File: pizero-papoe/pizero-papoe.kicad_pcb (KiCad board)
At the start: 4 copper layers, 80 x 30 mm, 90 parts, among them IC1 RTL8153B-VB-CG, J1 PogoPin_01x01, J2 PogoPin_01x01, J3 PogoPin_01x01, J4 PogoPin_01x01, J5 PogoPin_01x01, J6 RJ45_LED_AK_Shielded, P1 USB_C_Plug_USB3.0_9P, Q2 DMMT3906_Dual_PNP, Q3 Q_PMOS_GSD, U1 93LC46B, U2 TPS63070RNMR, U3 MX25L3233FM1, U4 WE-TVS-82400102-dnp, Y1 25Mhz

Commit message: add JLC04162H-3313-stackup info
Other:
- board text added: "0"
- board text added: "0 mm"
- board text added: "0.01 mm"
- board text added: "0.0152 mm"
- board text added: "0.02"
- board text added: "0.035 mm"
- board text added: "0.0994 mm"
- board text added: "1"
- board text added: "1.265 mm"
- board text added: "3.3"
- board text added: "4.5"
- board text added: "B.Cu"
- board text added: "B.Mask"
- board text added: "B.Paste"
- board text added: "B.Silkscreen"
- board text added: "Bottom Silk Screen"
- board text added: "Bottom Solder Mask"
- board text added: "Bottom Solder Paste"
- board text added: "Color"
- board text added: "Dielectric 1"
- board text added: "Dielectric 2"
- board text added: "Dielectric 3"
- board text added: "Epsilon R"
- board text added: "F.Cu"
- board text added: "F.Mask"
- board text added: "F.Paste"
- board text added: "F.Silkscreen"
- board text added: "FR4"
- board text added: "In1.Cu"
- board text added: "In2.Cu"
- board text added: "Layer Name"
- board text added: "Loss Tangent"
- board text added: "Material"
- board text added: "Not specified"
- board text added: "Thickness (mm)"
- board text added: "Top Silk Screen"
- board text added: "Top Solder Mask"
- board text added: "Top Solder Paste"
- board text added: "Type"
- board text added: "copper"
- board text added: "core"
- board text added: "prepreg"

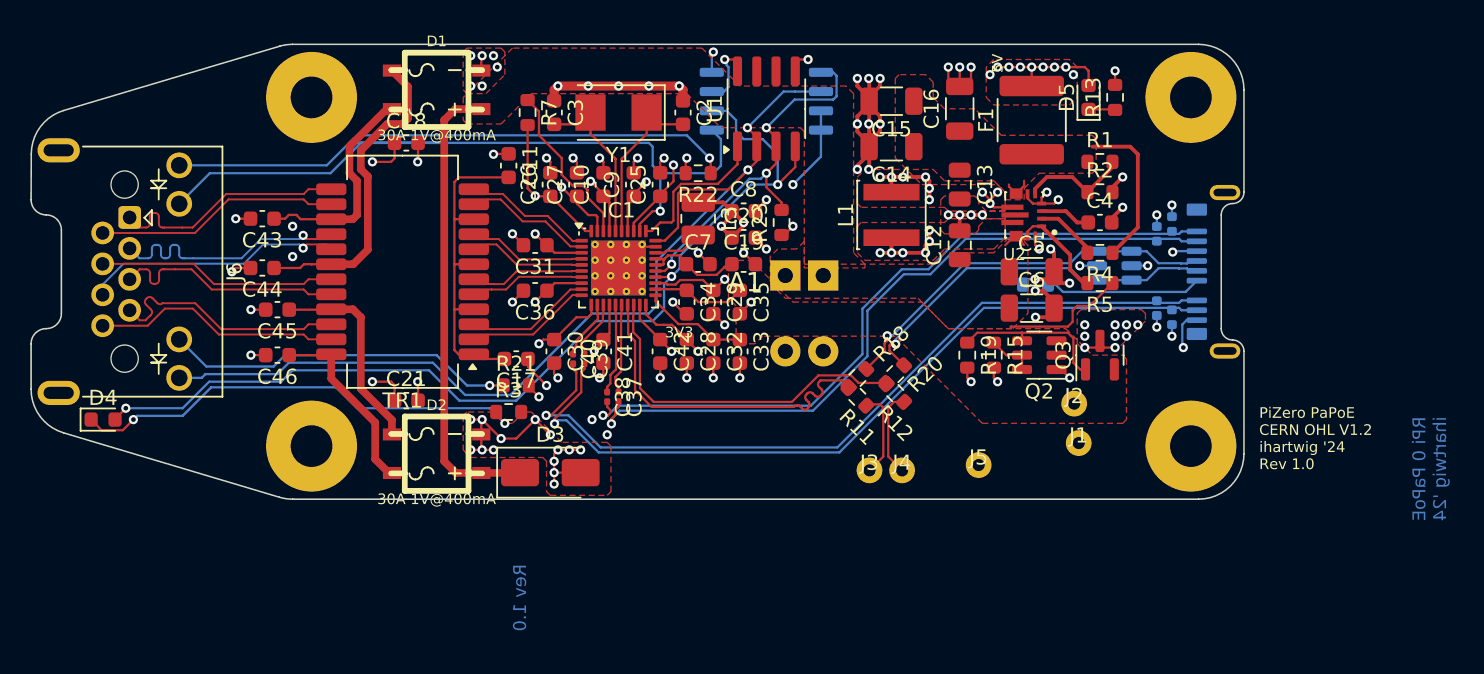
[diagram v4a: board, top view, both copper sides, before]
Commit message: pizero-papoe sch pcb fixes and cleanup
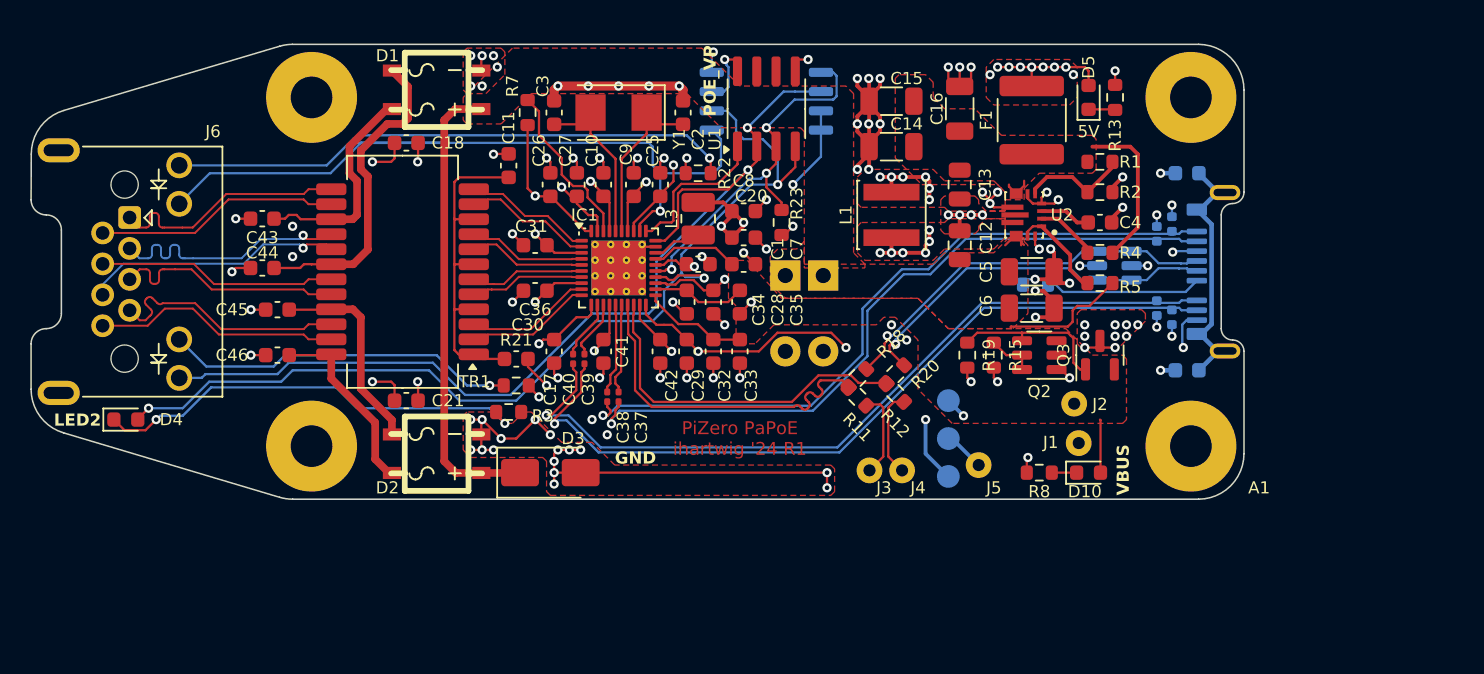
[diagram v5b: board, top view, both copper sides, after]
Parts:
- added C1: 0.1uf, Capacitor_SMD:C_0603_1608Metric, F.Cu at (135.1, 92.2)
- added C22: 1uF, Capacitor_SMD:C_0603_1608Metric, B.Cu at (167.3, 86.2)
- added D10: LED Green, LED_SMD:LED_0603_1608Metric, F.Cu at (160.8, 106.0)
- added R8: 1k, Resistor_SMD:R_0603_1608Metric, F.Cu at (157.6, 106.0)
- added TP1: VBUS, TestPoint:TestPoint_Pad_D1.5mm, B.Cu at (151.6, 101.2)
- added TP2: GND, TestPoint:TestPoint_Pad_D1.5mm, B.Cu at (151.6, 103.7)
- added TP3: 3V3, TestPoint:TestPoint_Pad_D1.5mm, B.Cu at (151.6, 106.2)
- C18, C21: value 1nF -> 1uF
- C19: value 4.7uF -> 1uF; moved to B.Cu
- C29: value 0.1uf -> 4.7uF
- moved C19 30.1 mm to (167.3, 99.2), turned to 180 degrees
- moved C28 3.69 mm to (136.1, 94.7)
- moved C29 3.69 mm to (134.3, 98.0)
- moved C7 3.00 mm to (138.1, 92.2)
- moved D4 1.50 mm to (97.3, 102.5)
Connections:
- C19 pad 1: /RPI_VBUS -> /P1_SH
- IC1 pad 26: /RPI_VBUS -> +3V3
- P1 pad SH1: (no net) -> /P1_SH
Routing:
- net +3V3: track 51.1 -> 81.4 mm, vias 9 -> 12
- net GND: track 124.7 -> 153.9 mm, vias 89 -> 96
- net /P1_SH: track 0.00 -> 18.4 mm
- net /RPI_VBUS: track 14.9 -> 18.0 mm, vias 0 -> 1
- net /IC1_EED0_LED2: track 65.3 -> 67.9 mm
- net Net-(D10-K): track 0.00 -> 1.64 mm
- net Net-(D4-K): track 30.7 -> 29.2 mm
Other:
- board text added: "GND"
- board text added: "LED0"
- board text added: "LED1"
- board text added: "LED2"
- board text added: "POE_VP"
- board text added: "PiZero PaPoE CERN OHL V1.2 ihartwig '24 R1"
- board text added: "PiZero PaPoE ihartwig '24 R1"
- board text added: "USB C Plug"
- board text added: "VBUS"
- board text removed: "3V3"
- board text removed: "PiZero PaPoE CERN OHL V1.2 ihartwig '24 Rev 1.0"
- board text removed: "RPi 0 PaPoE ihartwig '24"
- board text removed: "Rev 1.0"
